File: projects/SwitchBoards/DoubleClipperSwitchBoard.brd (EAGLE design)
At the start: 18.7 x 14.6 mm, 9 parts

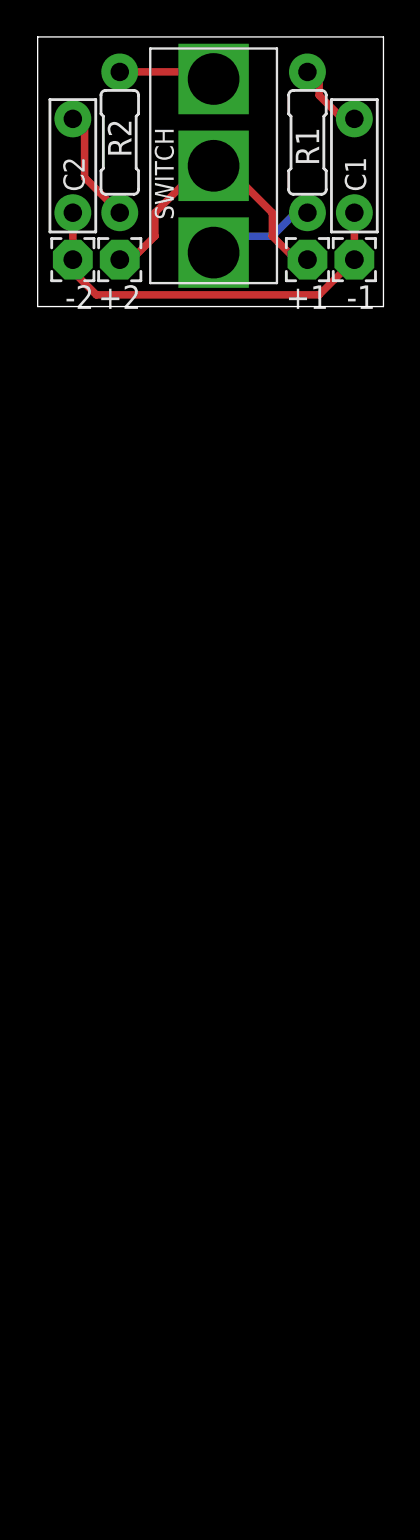
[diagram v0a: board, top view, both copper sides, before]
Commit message: Added clipper boards, filter board update.
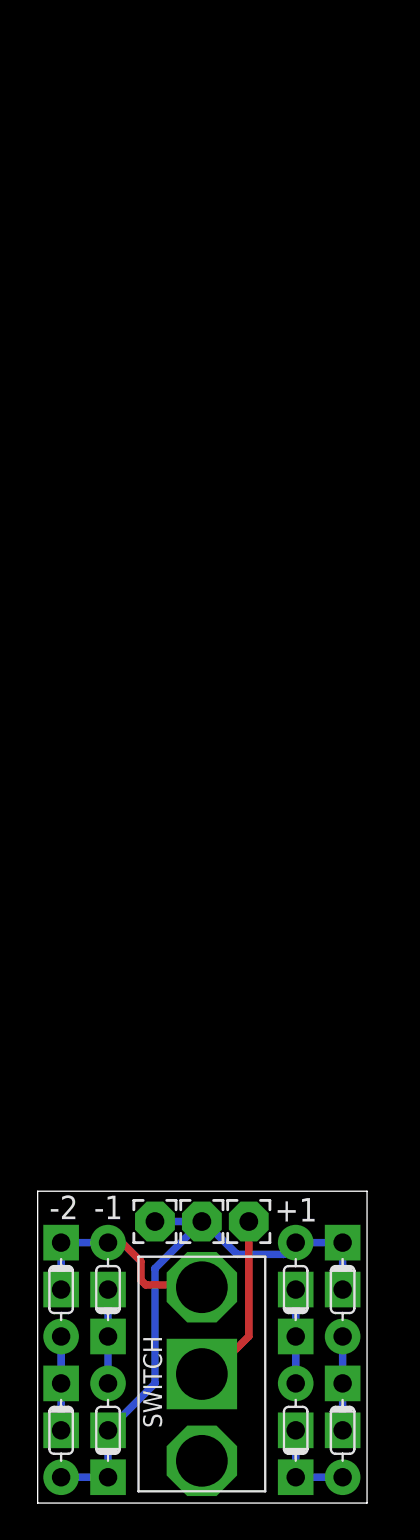
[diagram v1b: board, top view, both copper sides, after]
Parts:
- removed +2: (no value), wirepad:2,15/1,0
- removed C1, C2: (no value), capacitors-film:BOX_SMALL
- removed R1, R2: (no value), resistors:R0207/3
- added D1, D2, D3, D4, U$4, U$5, U$8, U$9: CLIPPER_BLOCK, gc_pedal_parts:CLIPPER_BLOCK
- moved U$1 65.4 mm to (8.89, 6.99)
- moved -1 52.7 mm to (8.89, 15.2), turned to 0 degrees
- moved -2 52.3 mm to (6.35, 15.2), turned to 0 degrees
- moved +1 52.2 mm to (11.4, 15.2), turned to 0 degrees
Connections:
- new net N$6: D2.P$3, D4.P$1, D4.P$2
- new net N$8: U$5.P$1, U$5.P$2, U$9.P$3
- net N$1: now also +1.1, U$1.P$3; no longer R1.1, U$1.P$1
- net N$2: now also U$4.P$3, U$8.P$1, U$8.P$2; no longer C1.2, R1.2
- net N$3: now also D1.P$3, D2.P$1, D2.P$2, U$1.P$1; no longer C2.2, R2.2
- net N$4: now also D1.P$1, D1.P$2, D3.P$3; no longer R2.1, U$1.P$2
- net N$5: now also U$1.P$2, U$4.P$1, U$4.P$2, U$5.P$3; no longer -1.1, -2.1, C1.1, C2.1
- net N$7: now also -1.1, -2.1, D3.P$1, D3.P$2, D4.P$3, U$8.P$3, U$9.P$1, U$9.P$2; no longer +1.1, +2.1, U$1.P$3
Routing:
- net N$7: track 15.9 -> 32.2 mm
- net N$5: track 22.3 -> 11.8 mm
- net N$8: track 0.00 -> 5.08 mm
- net N$6: track 0.00 -> 5.08 mm
- net N$1: track 6.06 -> 9.60 mm
- net N$3: track 6.50 -> 5.08 mm
- net N$2: track 4.34 -> 5.08 mm
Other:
- board size 18.7 x 14.6 mm -> 17.8 x 16.9 mm
- board text added: "DoubleClipperSwitch"
- board text added: "GJCAMANN1/2014"
- board text removed: "FilterSwitchBoard"
- board text removed: "GJCAMANN2014"

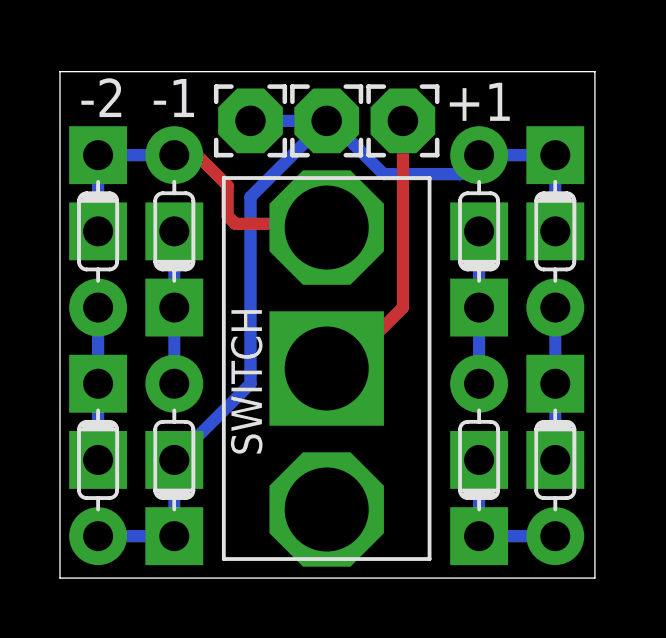
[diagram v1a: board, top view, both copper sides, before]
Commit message: Pass OSHPark DRC.
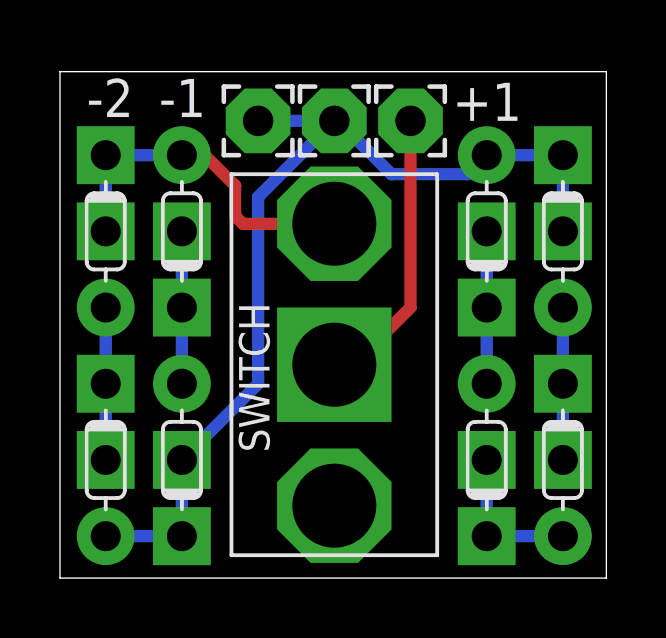
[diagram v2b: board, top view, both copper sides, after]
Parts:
- moved U$1 0.28 mm to (9.14, 7.11)
- moved -2 0.25 mm to (6.60, 15.2)
- moved U$4 0.25 mm to (1.52, 11.6)
- moved U$5 0.25 mm to (4.06, 11.6)
- moved U$8 0.25 mm to (1.52, 3.94)
- moved U$9 0.25 mm to (4.06, 3.94)
- moved +1 0.25 mm to (11.7, 15.2)
- moved -1 0.25 mm to (9.14, 15.2)
- moved D2 0.25 mm to (14.2, 3.94)
- moved D4 0.25 mm to (14.2, 11.6)
- moved D1 0.25 mm to (16.8, 3.94)
- moved D3 0.25 mm to (16.8, 11.6)
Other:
- board size 17.8 x 16.9 mm -> 18.2 x 16.9 mm

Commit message: Final project updates. Ready to send to oshpark.
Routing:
- net N$3: track 5.08 -> 10.2 mm
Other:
- board text added: "GJCAMANN(C)2014"
- board text added: "V1.0"
- board text removed: "GJCAMANN1/2014"
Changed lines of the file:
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@@
 <layer number="27" name="tValues" color="7" fill="1" visible="yes" active="yes"/>
 <layer number="28" name="bValues" color="7" fill="1" visible="yes" active="yes"/>
-<layer number="29" name="tStop" color="7" fill="3" visible="no" active="yes"/>
-<layer number="30" name="bStop" color="7" fill="6" visible="no" active="yes"/>
-<layer number="31" name="tCream" color="7" fill="4" visible="no" active="yes"/>
-<layer number="32" name="bCream" color="7" fill="5" visible="no" active="yes"/>
-<layer number="33" name="tFinish" color="6" fill="3" visible="no" active="yes"/>
-<layer number="34" name="bFinish" color="6" fill="6" visible="no" active="yes"/>
-<layer number="35" name="tGlue" color="7" fill="4" visible="no" active="yes"/>
-<layer number="36" name="bGlue" color="7" fill="5" visible="no" active="yes"/>
-<layer number="37" name="tTest" color="7" fill="1" visible="no" active="yes"/>
-<layer number="38" name="bTest" color="7" fill="1" visible="no" active="yes"/>
+<layer number="29" name="tStop" color="7" fill="3" visible="yes" active="yes"/>
+<layer number="30" name="bStop" color="7" fill="6" visible="yes" active="yes"/>
+<layer number="31" name="tCream" color="7" fill="4" visible="yes" active="yes"/>
+<layer number="32" name="bCream" color="7" fill="5" visible="yes" active="yes"/>
+<layer number="33" name="tFinish" color="6" fill="3" visible="yes" active="yes"/>
+<layer number="34" name="bFinish" color="6" fill="6" visible="yes" active="yes"/>
+<layer number="35" name="tGlue" color="7" fill="4" visible="yes" active="yes"/>
+<layer number="36" name="bGlue" color="7" fill="5" visible="yes" active="yes"/>
+<layer number="37" name="tTest" color="7" fill="1" visible="yes" active="yes"/>
+<layer number="38" name="bTest" color="7" fill="1" visible="yes" active="yes"/>
 <layer number="39" name="tKeepout" color="4" fill="11" visible="yes" active="yes"/>
 <layer number="40" name="bKeepout" color="1" fill="11" visible="yes" active="yes"/>
@@
 <layer number="42" name="bRestrict" color="1" fill="10" visible="yes" active="yes"/>
 <layer number="43" name="vRestrict" color="2" fill="10" visible="yes" active="yes"/>
-<layer number="44" name="Drills" color="7" fill="1" visible="no" active="yes"/>
-<layer number="45" name="Holes" color="7" fill="1" visible="no" active="yes"/>
-<layer number="46" name="Milling" color="3" fill="1" visible="no" active="yes"/>
-<layer number="47" name="Measures" color="7" fill="1" visible="no" active="yes"/>
+<layer number="44" name="Drills" color="7" fill="1" visible="yes" active="yes"/>
+<layer number="45" name="Holes" color="7" fill="1" visible="yes" active="yes"/>
+<layer number="46" name="Milling" color="3" fill="1" visible="yes" active="yes"/>
+<layer number="47" name="Measures" color="7" fill="1" visible="yes" active="yes"/>
 <layer number="48" name="Document" color="7" fill="1" visible="yes" active="yes"/>
 <layer number="49" name="Reference" color="7" fill="1" visible="yes" active="yes"/>
@@
 <wire x1="18.212" y1="16.881" x2="0" y2="16.881" width="0" layer="20"/>
 <wire x1="0" y1="16.881" x2="0" y2="0" width="0" layer="20"/>
-<text x="11.43" y="0.889" size="1.016" layer="22" rot="MR90">GJCAMANN1/2014</text>
+<text x="11.43" y="0.889" size="1.016" layer="22" rot="MR90">GJCAMANN(C)2014</text>
 <text x="5.842" y="0.254" size="1.016" layer="22" rot="MR90">DoubleClipperSwitch</text>
+<text x="17.78" y="15.24" size="1.016" layer="22" rot="MR0">V1.0</text>
+<wire x1="5.334" y1="11.684" x2="6.858" y2="11.684" width="0.4064" layer="21"/>
+<wire x1="6.477" y1="12.065" x2="6.858" y2="11.684" width="0.4064" layer="21"/>
+<wire x1="6.858" y1="11.684" x2="6.477" y2="11.303" width="0.4064" layer="21"/>
+<wire x1="12.954" y1="2.413" x2="11.557" y2="2.413" width="0.4064" layer="21"/>
+<wire x1="11.938" y1="2.794" x2="11.557" y2="2.413" width="0.4064" layer="21"/>
+<wire x1="11.938" y1="2.032" x2="11.557" y2="2.413" width="0.4064" layer="21"/>
+<wire x1="10.287" y1="16.383" x2="10.033" y2="16.637" width="0.4064" layer="21"/>
+<wire x1="10.033" y1="16.637" x2="5.715" y2="16.637" width="0.4064" layer="21"/>
+<wire x1="5.715" y1="16.637" x2="5.461" y2="16.383" width="0.4064" layer="21"/>
 </plain>
 <attributes>
@@
 <contactref element="U$1" pad="P$1"/>
 <wire x1="14.224" y1="1.397" x2="16.764" y2="1.397" width="0.4064" layer="16"/>
-<wire x1="14.224" y1="1.397" x2="14.224" y2="3.937" width="0.4064" layer="16"/>
-<wire x1="9.144" y1="2.413" x2="14.224" y2="3.937" width="0" layer="19" extent="1-1"/>
+<wire x1="14.224" y1="1.397" x2="14.224" y2="2.413" width="0.4064" layer="16"/>
+<wire x1="14.224" y1="2.54" x2="14.224" y2="3.937" width="0.4064" layer="16"/>
+<wire x1="9.144" y1="2.413" x2="14.224" y2="2.413" width="0.4064" layer="16"/>
+<wire x1="14.224" y1="2.413" x2="14.224" y2="2.54" width="0.4064" layer="16"/>
 </signal>
 <signal name="N$4">
